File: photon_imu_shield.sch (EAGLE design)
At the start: 29 parts, among them U1 LSM9DS1

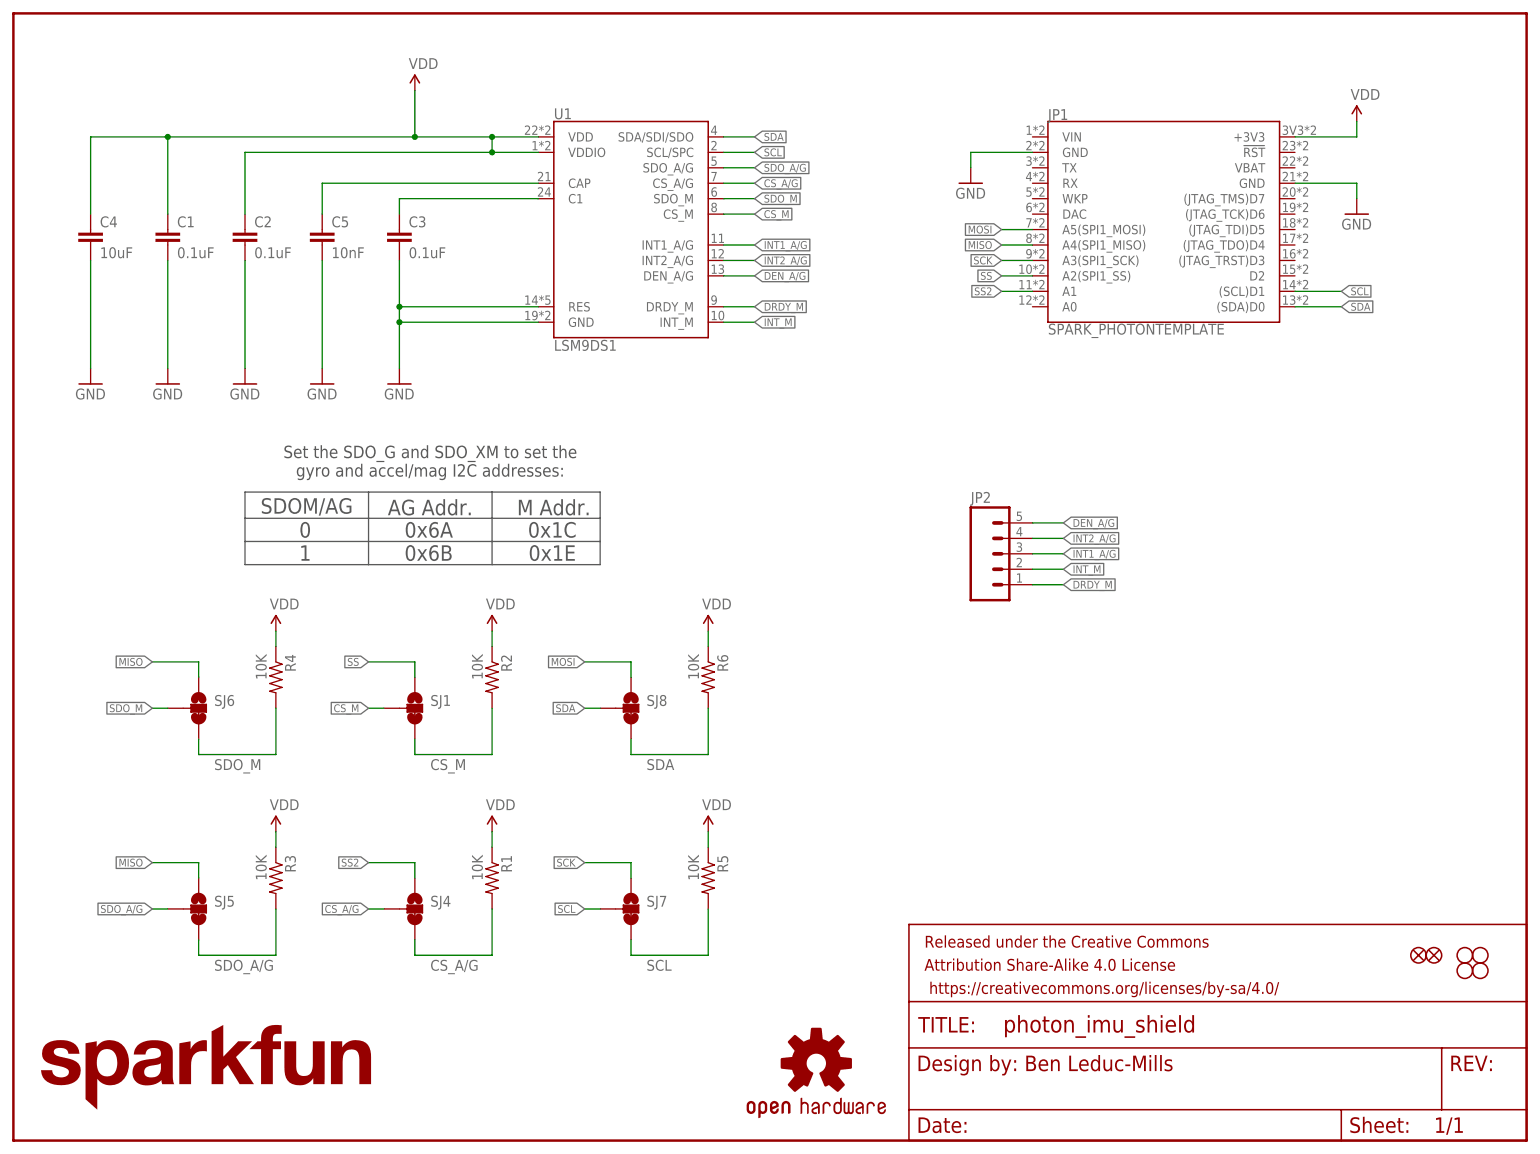
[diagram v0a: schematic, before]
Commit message: Fixed silk, added switch vias
Not adding JST, b/c pins are adjacent so can just solder to them.
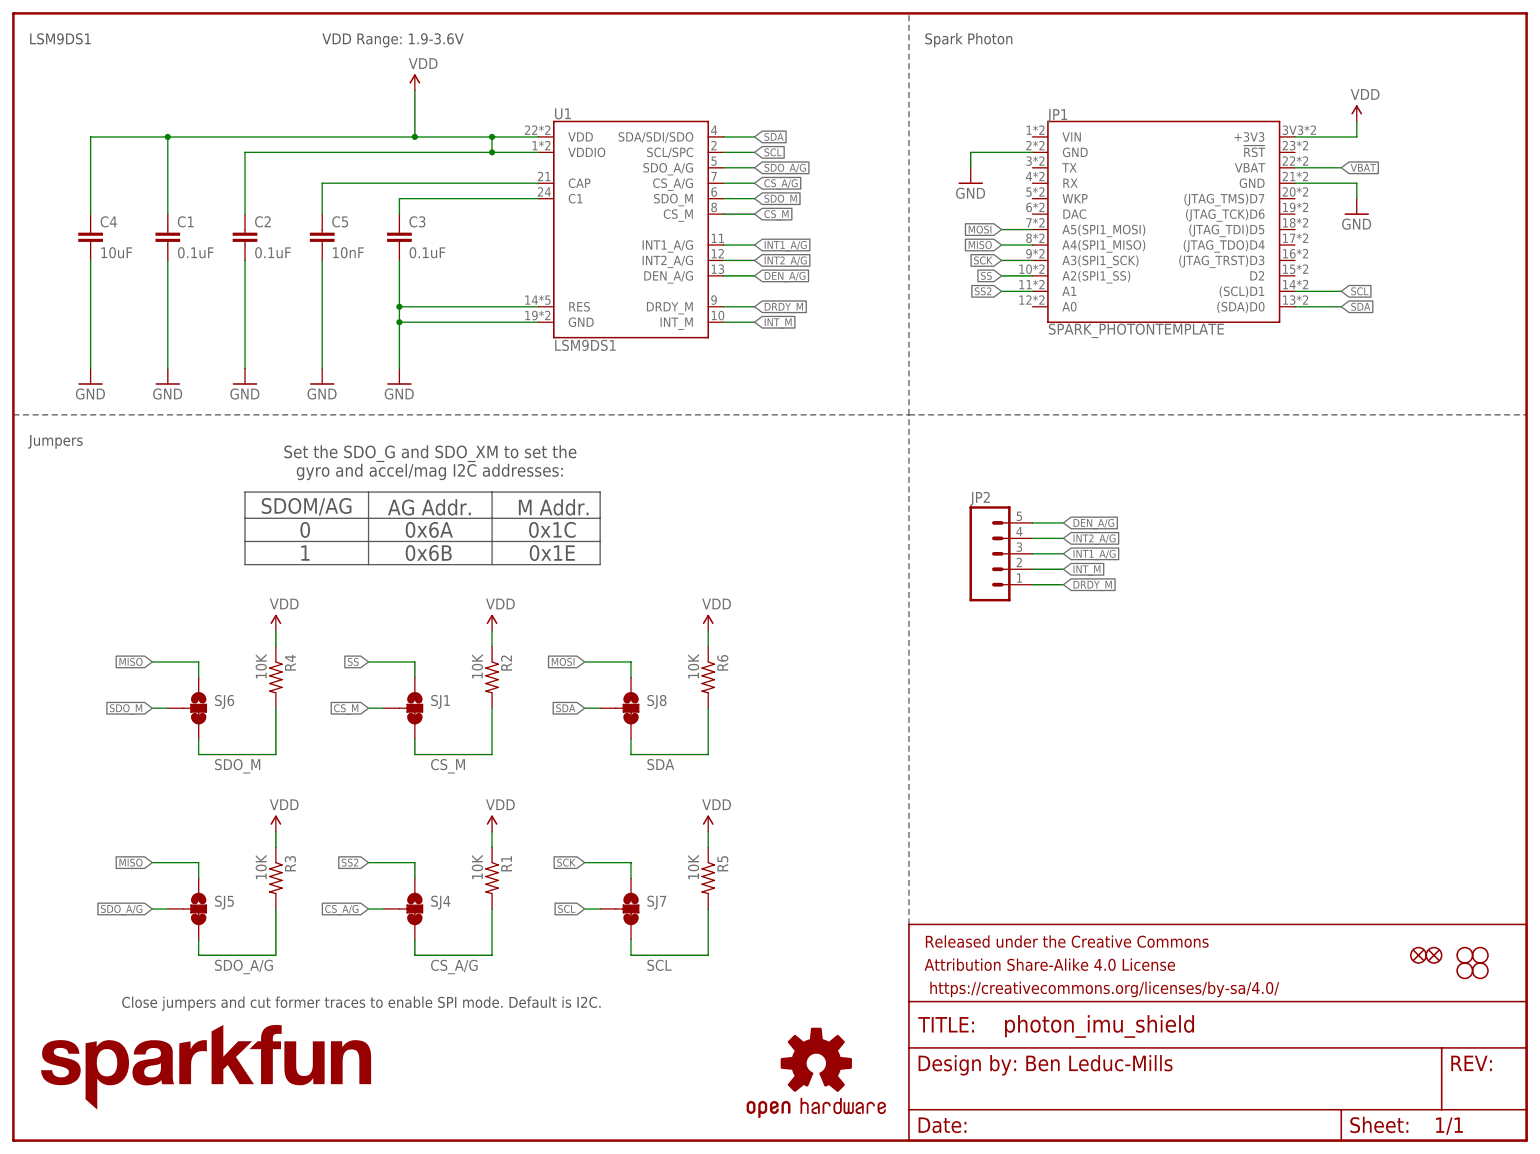
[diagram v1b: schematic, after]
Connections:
- new net VBAT: JP1.VBAT
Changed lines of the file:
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@@
 <sheet>
 <plain>
-<text x="17.78" y="21.844" size="1.778" layer="150">Close jumpers and cut former traces to enable SPI mode. Default is I2C.</text>
-<wire x1="0" y1="119.38" x2="147.32" y2="119.38" width="0.1524" layer="150" style="longdash"/>
-<wire x1="147.32" y1="119.38" x2="147.32" y2="185.42" width="0.1524" layer="150" style="longdash"/>
-<wire x1="147.32" y1="35.56" x2="147.32" y2="119.38" width="0.1524" layer="150" style="longdash"/>
-<text x="50.8" y="180.34" size="1.778" layer="150">VDD Range: 1.9-3.6V</text>
-<text x="2.54" y="180.34" size="1.778" layer="150">LSM9DS1</text>
-<text x="149.86" y="180.34" size="1.778" layer="150">Spark Photon</text>
-<text x="2.54" y="114.3" size="1.778" layer="150">Jumpers</text>
+<text x="17.78" y="21.844" size="1.778" layer="97">Close jumpers and cut former traces to enable SPI mode. Default is I2C.</text>
+<wire x1="0" y1="119.38" x2="147.32" y2="119.38" width="0.1524" layer="97" style="longdash"/>
+<wire x1="147.32" y1="119.38" x2="147.32" y2="185.42" width="0.1524" layer="97" style="longdash"/>
+<wire x1="147.32" y1="35.56" x2="147.32" y2="119.38" width="0.1524" layer="97" style="longdash"/>
+<text x="50.8" y="180.34" size="1.778" layer="97">VDD Range: 1.9-3.6V</text>
+<text x="2.54" y="180.34" size="1.778" layer="97">LSM9DS1</text>
+<text x="149.86" y="180.34" size="1.778" layer="97">Spark Photon</text>
+<text x="2.54" y="114.3" size="1.778" layer="97">Jumpers</text>
 <text x="48.26" y="104.394" size="2.54" layer="97" align="center">SDOM/AG</text>
 <text x="88.646" y="98.552" size="2.54" layer="97" align="center">0x1C
@@
 <text x="68.58" y="111.76" size="2.032" layer="97" align="center">Set the SDO_G and SDO_XM to set the
 gyro and accel/mag I2C addresses:</text>
-<wire x1="147.32" y1="119.38" x2="248.92" y2="119.38" width="0.2032" layer="150" style="longdash"/>
+<wire x1="147.32" y1="119.38" x2="248.92" y2="119.38" width="0.2032" layer="97" style="longdash"/>
 <text x="149.86" y="114.3" size="1.778" layer="150">Header</text>
 </plain>
@@
 <pinref part="SJ8" gate="G$1" pin="3"/>
 <wire x1="114.3" y1="63.5" x2="114.3" y2="71.12" width="0.1524" layer="91"/>
-<label x="104.14" y="60.96" size="1.778" layer="95"/>
+<label x="104.14" y="60.96" size="1.778" layer="97"/>
 <wire x1="101.6" y1="66.04" x2="101.6" y2="63.5" width="0.1524" layer="91"/>
 <wire x1="101.6" y1="63.5" x2="114.3" y2="63.5" width="0.1524" layer="91"/>
@@
 <pinref part="R5" gate="G$1" pin="2"/>
 <wire x1="114.3" y1="30.48" x2="114.3" y2="38.1" width="0.1524" layer="91"/>
-<label x="104.14" y="27.94" size="1.778" layer="95"/>
+<label x="104.14" y="27.94" size="1.778" layer="97"/>
 <wire x1="101.6" y1="33.02" x2="101.6" y2="30.48" width="0.1524" layer="91"/>
 <wire x1="101.6" y1="30.48" x2="114.3" y2="30.48" width="0.1524" layer="91"/>
@@
 <wire x1="43.18" y1="38.1" x2="43.18" y2="30.48" width="0.1524" layer="91"/>
 <pinref part="SJ5" gate="G$1" pin="3"/>
-<label x="33.02" y="27.94" size="1.778" layer="95"/>
+<label x="33.02" y="27.94" size="1.778" layer="97"/>
 <wire x1="30.48" y1="33.02" x2="30.48" y2="30.48" width="0.1524" layer="91"/>
 <wire x1="30.48" y1="30.48" x2="43.18" y2="30.48" width="0.1524" layer="91"/>
@@
 <pinref part="R1" gate="G$1" pin="2"/>
 <wire x1="78.74" y1="38.1" x2="78.74" y2="30.48" width="0.1524" layer="91"/>
-<label x="68.58" y="27.94" size="1.778" layer="95"/>
+<label x="68.58" y="27.94" size="1.778" layer="97"/>
 <wire x1="66.04" y1="33.02" x2="66.04" y2="30.48" width="0.1524" layer="91"/>
 <wire x1="66.04" y1="30.48" x2="78.74" y2="30.48" width="0.1524" layer="91"/>
@@
 <wire x1="43.18" y1="71.12" x2="43.18" y2="63.5" width="0.1524" layer="91"/>
 <pinref part="SJ6" gate="G$1" pin="3"/>
-<label x="33.02" y="60.96" size="1.778" layer="95"/>
+<label x="33.02" y="60.96" size="1.778" layer="97"/>
 <wire x1="30.48" y1="66.04" x2="30.48" y2="63.5" width="0.1524" layer="91"/>
 <wire x1="30.48" y1="63.5" x2="43.18" y2="63.5" width="0.1524" layer="91"/>
@@
 <pinref part="R2" gate="G$1" pin="2"/>
 <wire x1="78.74" y1="63.5" x2="78.74" y2="71.12" width="0.1524" layer="91"/>
-<label x="68.58" y="60.96" size="1.778" layer="95"/>
+<label x="68.58" y="60.96" size="1.778" layer="97"/>
 <wire x1="66.04" y1="66.04" x2="66.04" y2="63.5" width="0.1524" layer="91"/>
 <wire x1="66.04" y1="63.5" x2="78.74" y2="63.5" width="0.1524" layer="91"/>
@@
 </segment>
 </net>
+<net name="VBAT" class="0">
+<segment>
+<pinref part="JP1" gate="G$1" pin="VBAT"/>
+<wire x1="210.82" y1="160.02" x2="218.44" y2="160.02" width="0.1524" layer="91"/>
+<label x="218.44" y="160.02" size="1.27" layer="95" font="vector" xref="yes"/>
+</segment>
+</net>

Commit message: QC fixes
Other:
- note added: "v01"
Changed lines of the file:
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@@
 <wire x1="147.32" y1="119.38" x2="248.92" y2="119.38" width="0.2032" layer="97" style="longdash"/>
 <text x="149.86" y="114.3" size="1.778" layer="150">Header</text>
+<text x="238.76" y="7.62" size="2.54" layer="94" font="vector" ratio="10">v01</text>
 </plain>
 <instances>

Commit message: Adding gap between Photon and pin breakouts.
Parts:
- removed STANDOFF1, STANDOFF2, STANDOFF3, STANDOFF4: STAND-OFF, SparkFun-Electromechanical:STAND-OFF
- JP1: value SPARK_PHOTONTEMPLATE -> SPARK_PHOTONTEMPLATE_WIDE; device template_temp:SPARK_PHOTONTEMPLATE -> template_temp:SPARK_PHOTONTEMPLATE_WIDE
- LOGO1: value SFE_LOGO_NAME.1_INCH -> SFE_LOGO_NAME_FLAME.1_INCH; device SparkFun-Aesthetics:SFE_LOGO_NAME.1_INCH -> SparkFun-Aesthetics:SFE_LOGO_NAME_FLAME.1_INCH
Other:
- note added: "Set the SDO_AG and SDO_M to set the accel/gyro and mag I2C addresses:"
- note added: "v10"
- note removed: "Set the SDO_G and SDO_XM to set the gyro and accel/mag I2C addresses:"
- note removed: "v01"
